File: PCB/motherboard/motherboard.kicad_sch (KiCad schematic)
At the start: 0 parts

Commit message: schematic template added
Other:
- added sheet connectors (connectors.kicad_sch)
- added sheet power (power.kicad_sch)
- title: (none) -> MAIN

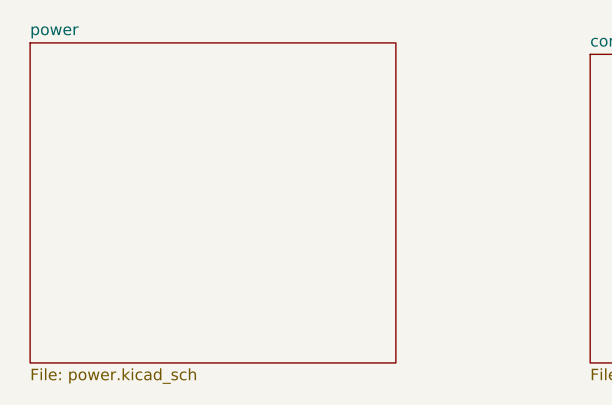
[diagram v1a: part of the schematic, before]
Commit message: started power schematic of pcb
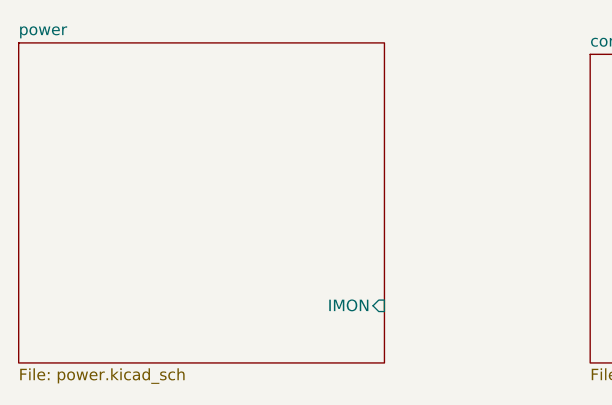
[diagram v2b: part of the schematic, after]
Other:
- sheet power ports: added IMON; removed none
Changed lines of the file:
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@@
 	)
 	(sheet
-		(at 85.09 49.53)
+		(at 83.82 49.53)
 		(size 40.64 35.56)
 		(exclude_from_sim no)
@@
 		)
 		(property "Sheetname" "power"
-			(at 85.09 48.8184 0)
+			(at 83.82 48.8184 0)
 			(effects
 				(font
@@
 		)
 		(property "Sheetfile" "power.kicad_sch"
-			(at 85.09 85.6746 0)
+			(at 83.82 85.6746 0)
 			(effects
 				(font
@@
 			)
 		)
+		(pin "IMON" input
+			(at 124.46 78.74 0)
+			(effects
+				(font
+					(size 1.27 1.27)
+				)
+				(justify right)
+			)
+		)

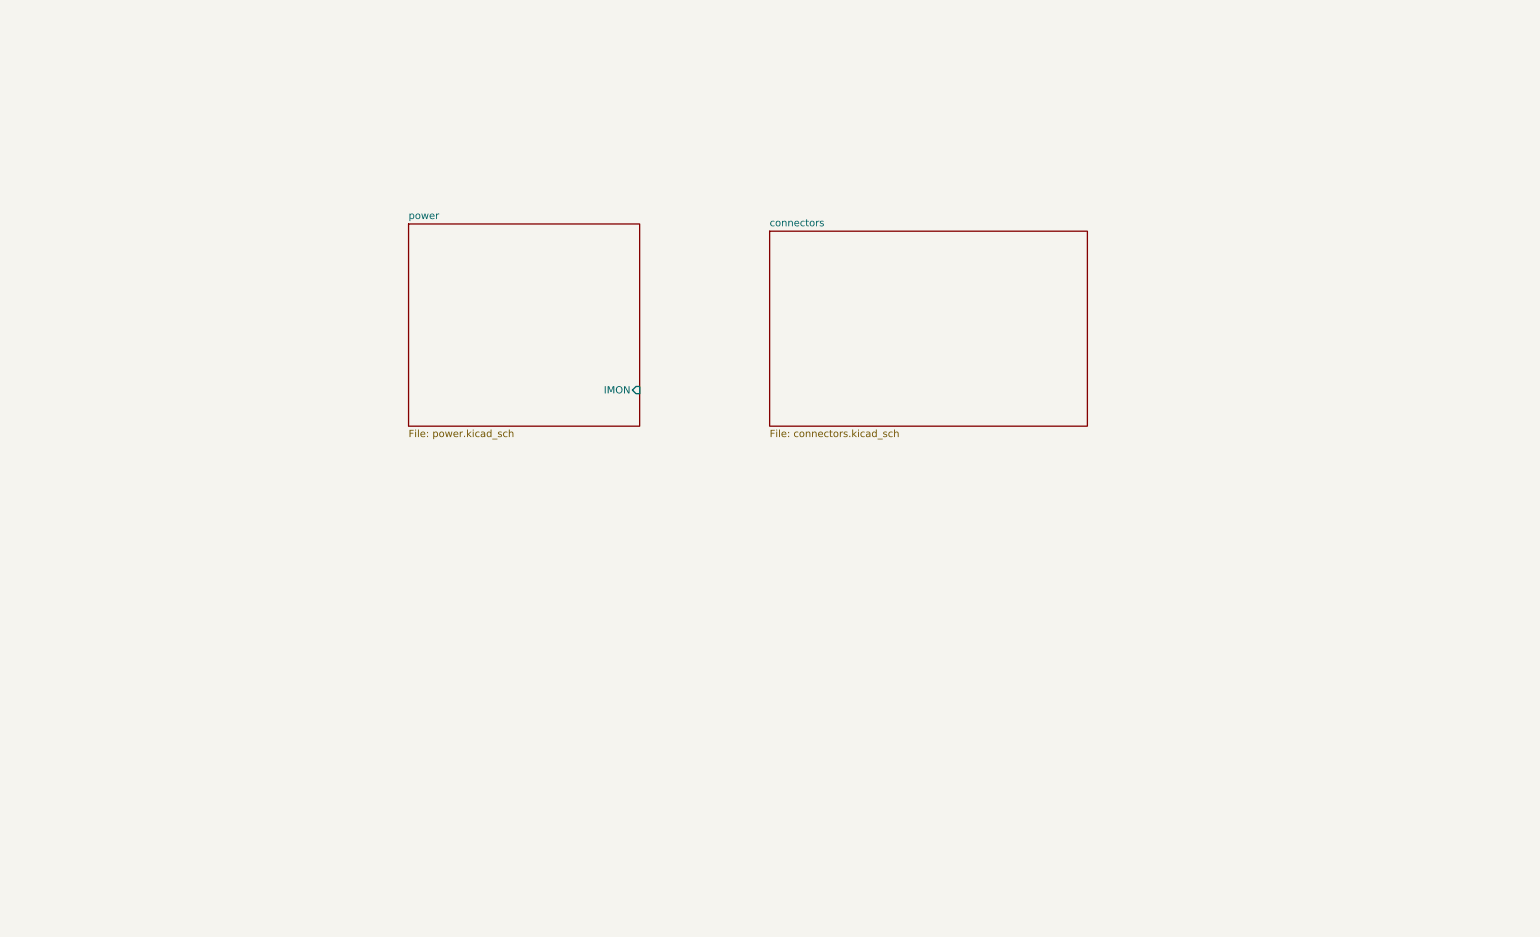
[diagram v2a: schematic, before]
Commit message: updated sch power
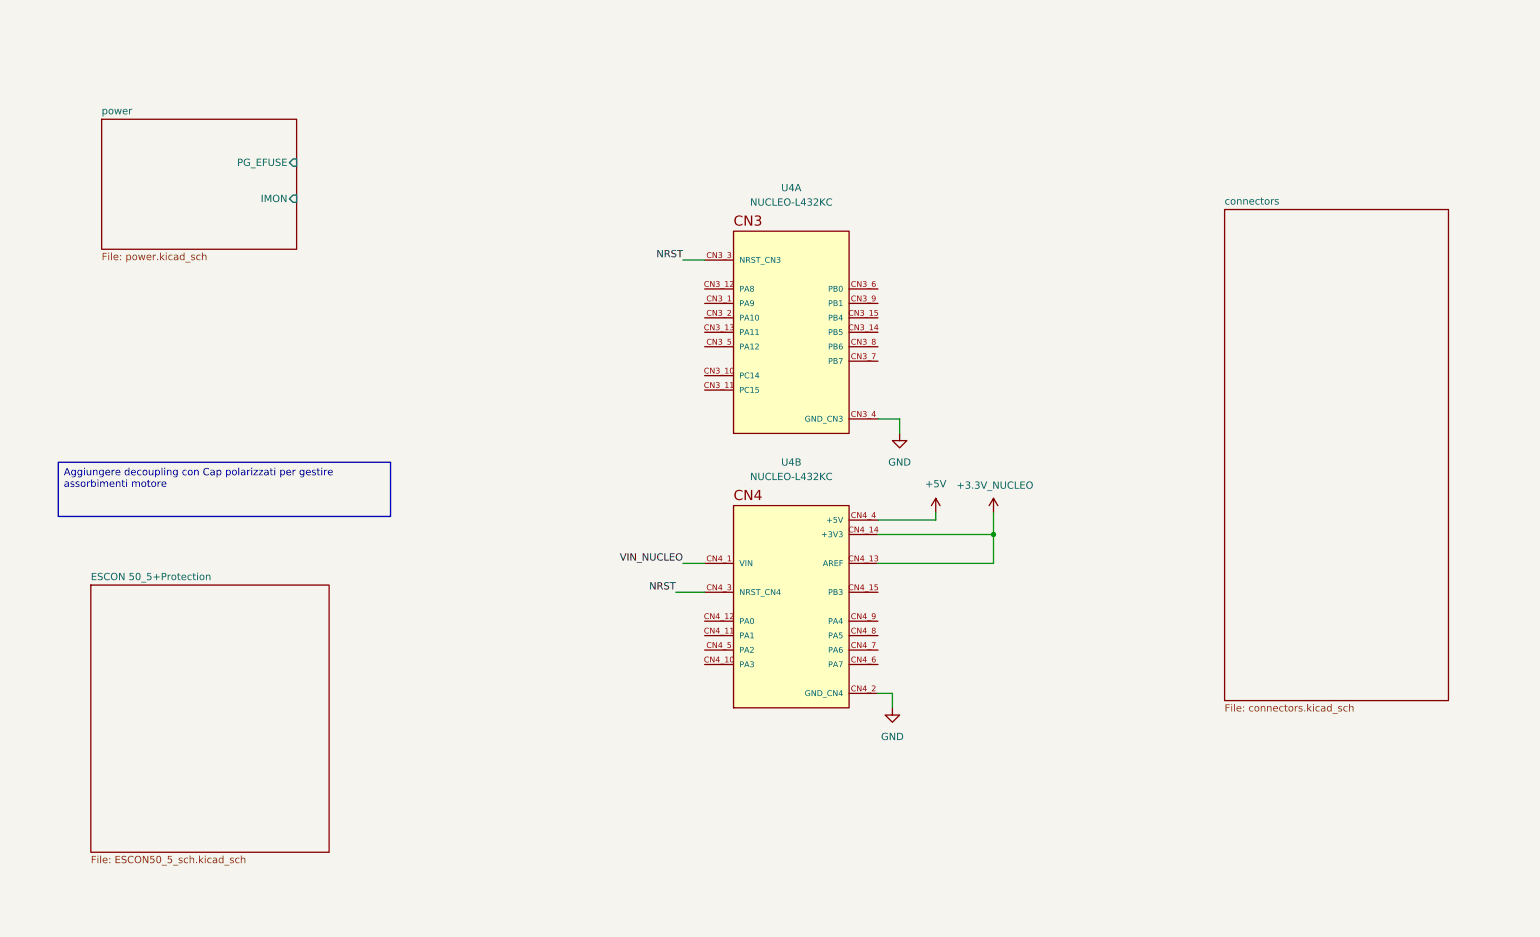
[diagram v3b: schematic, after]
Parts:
- added U4: NUCLEO-L432KC, NUCLEO-L432KC:MODULE_NUCLEO-L432KC, symbol NUCLEO-L432KC:NUCLEO-L432KC
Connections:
- new net +3.3V_NUCLEO: U4.CN4_13 (AREF), U4.CN4_14 (+3V3)
- new net +5V: U4.CN4_4 (+5V)
- new net GND: U4.CN3_4 (GND_CN3), U4.CN4_2 (GND_CN4)
- new net NRST: U4.CN3_3 (NRST_CN3), U4.CN4_3 (NRST_CN4)
- new net VIN_NUCLEO: U4.CN4_1 (VIN)
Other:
- added sheet ESCON 50_5+Protection (ESCON50_5_sch.kicad_sch)
- sheet power ports: added PG_EFUSE; removed none

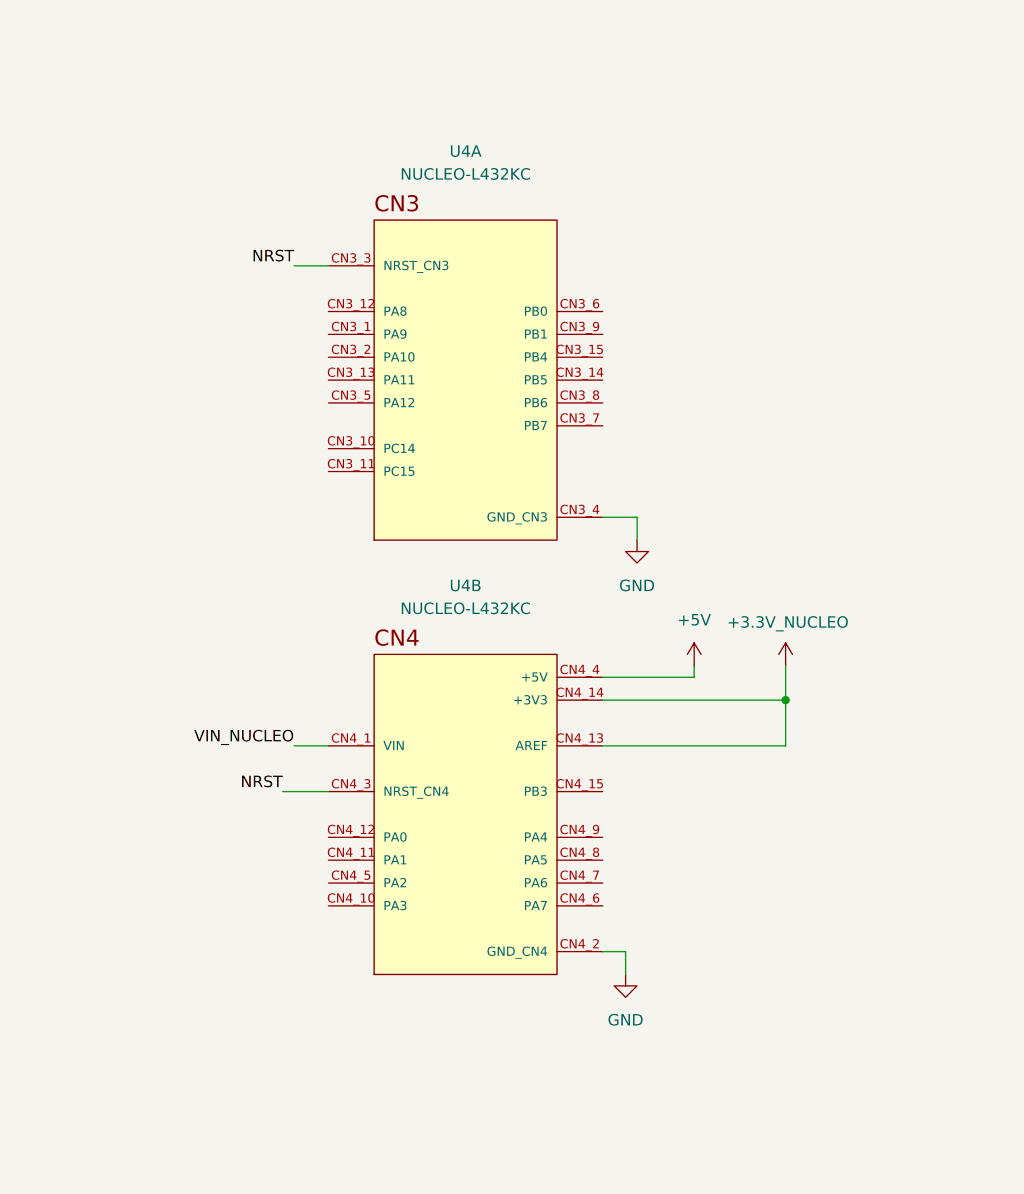
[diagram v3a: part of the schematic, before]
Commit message: aggiunto driver escon in libreria e nel progetto schematico
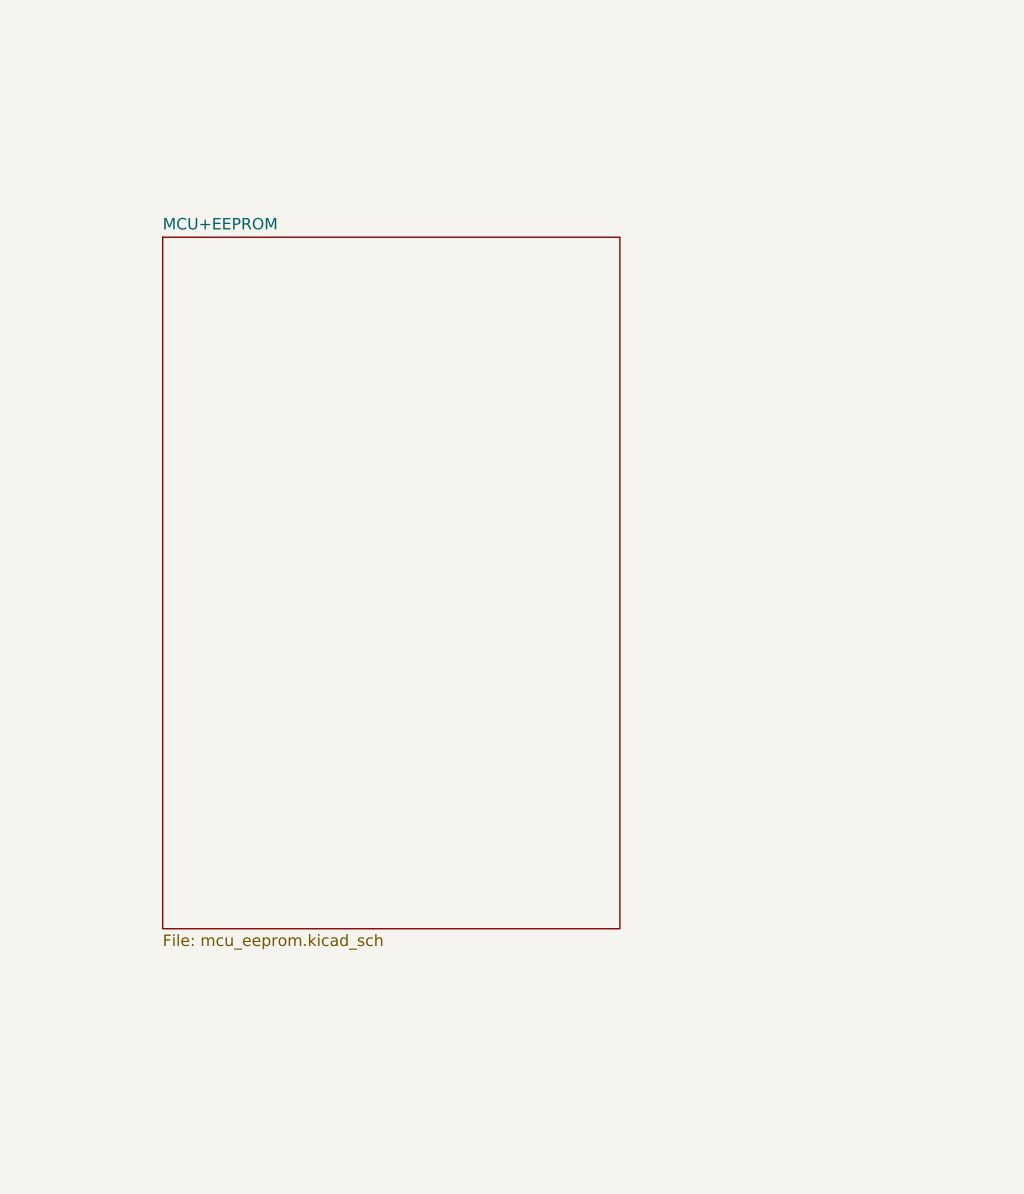
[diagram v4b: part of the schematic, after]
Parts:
- removed U4: NUCLEO-L432KC, NUCLEO-L432KC:MODULE_NUCLEO-L432KC, symbol NUCLEO-L432KC:NUCLEO-L432KC
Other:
- added sheet MCU+EEPROM (mcu_eeprom.kicad_sch)

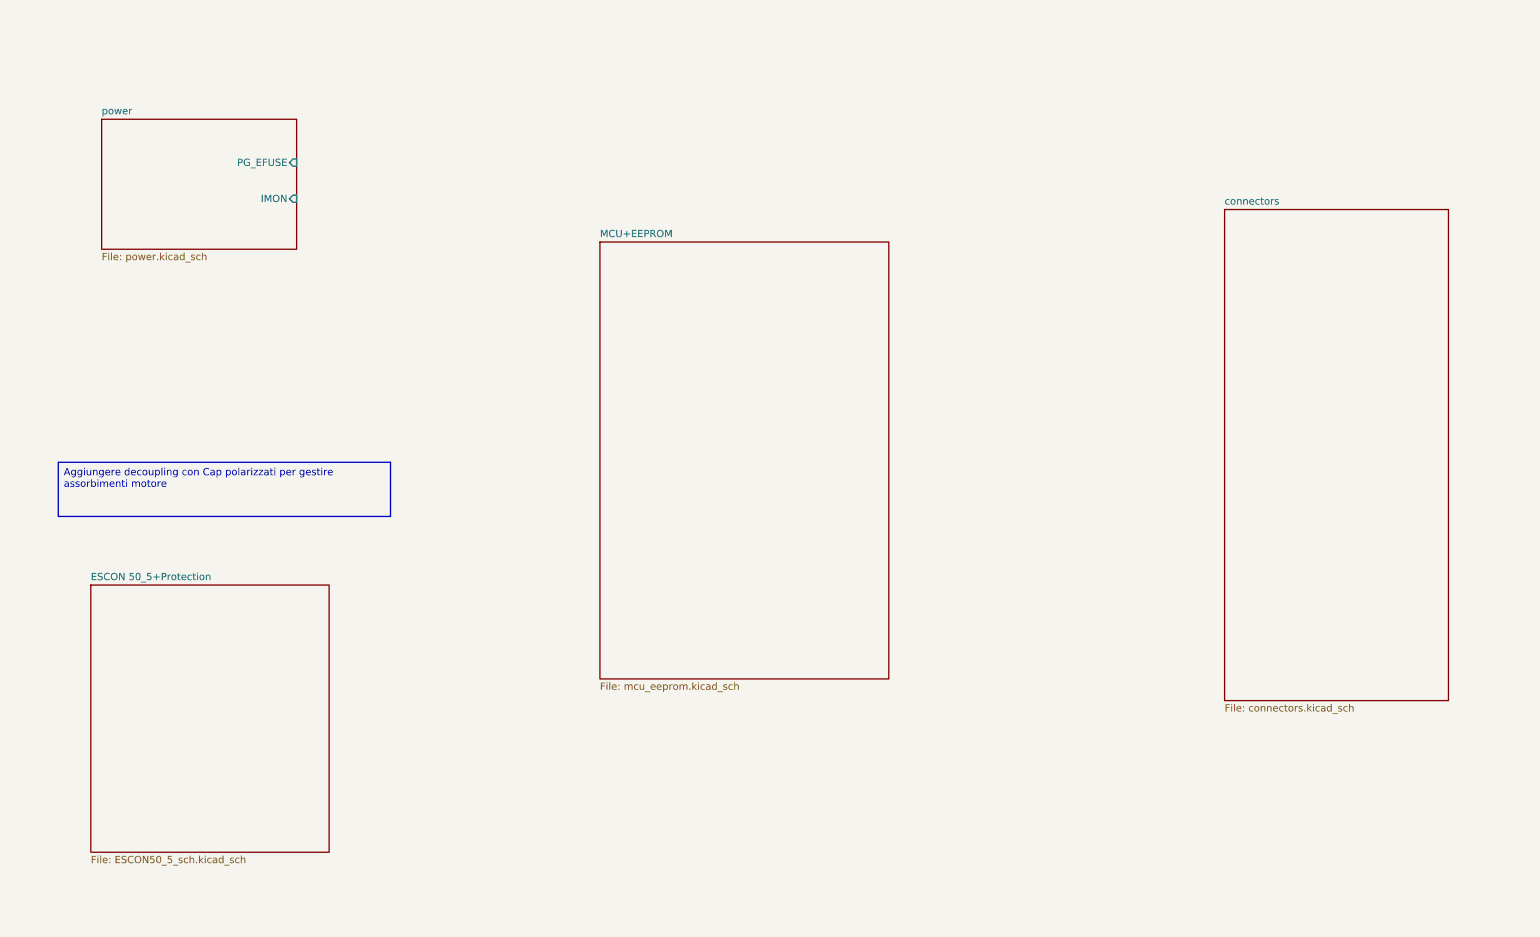
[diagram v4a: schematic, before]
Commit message: reverse current protection on ESCON+others
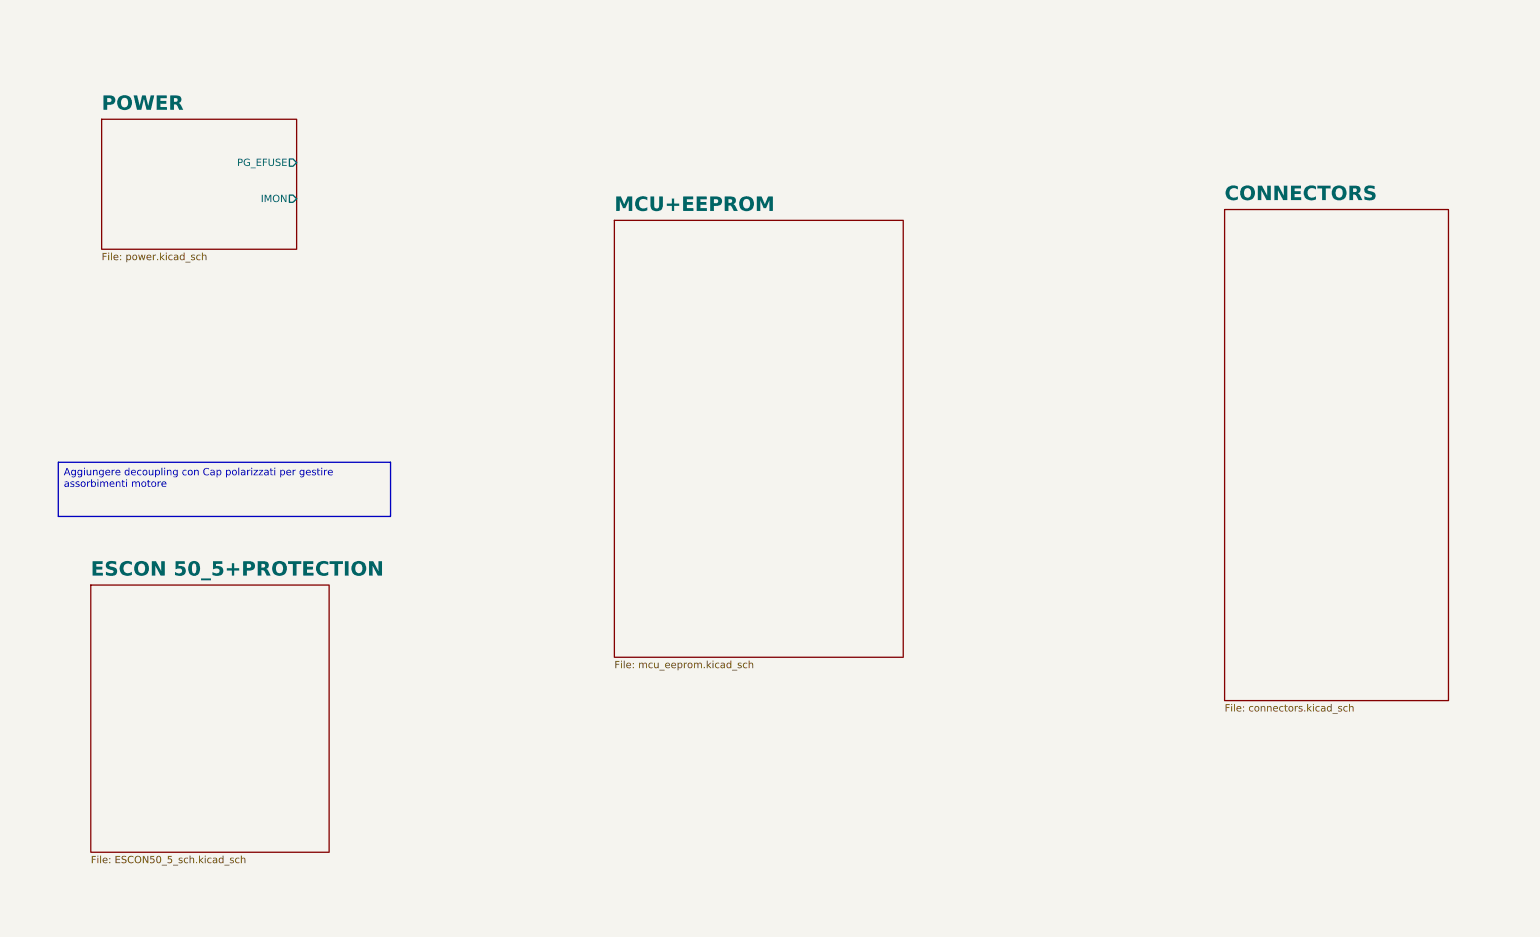
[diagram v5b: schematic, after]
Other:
- sheet ESCON 50_5+Protection renamed ESCON 50_5+PROTECTION
- sheet connectors renamed CONNECTORS
- sheet power renamed POWER
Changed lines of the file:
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@@
 			(color 245 255 30 1.0000)
 		)
-		(property "Sheetname" "ESCON 50_5+Protection"
-			(at 27.94 112.3184 0)
+		(property "Sheetname" "ESCON 50_5+PROTECTION"
+			(at 27.94 111.6834 0)
 			(effects
 				(font
-					(size 1.27 1.27)
+					(size 2.54 2.54)
+					(thickness 0.508)
+					(bold yes)
 				)
 				(justify left bottom)
@@
 			(color 39 240 255 1.0000)
 		)
-		(property "Sheetname" "connectors"
-			(at 227.33 46.2784 0)
+		(property "Sheetname" "CONNECTORS"
+			(at 227.33 45.6434 0)
 			(effects
 				(font
-					(size 1.27 1.27)
+					(size 2.54 2.54)
+					(thickness 0.508)
+					(bold yes)
 				)
 				(justify left bottom)
@@
 	)
 	(sheet
-		(at 117.475 52.705)
+		(at 120.015 48.895)
 		(size 50.8 76.835)
 		(exclude_from_sim no)
@@
 		)
 		(property "Sheetname" "MCU+EEPROM"
-			(at 117.475 51.9934 0)
+			(at 120.015 47.5484 0)
 			(effects
 				(font
-					(size 1.27 1.27)
+					(size 2.54 2.54)
+					(thickness 0.508)
+					(bold yes)
 				)
 				(justify left bottom)
@@
 		)
 		(property "Sheetfile" "mcu_eeprom.kicad_sch"
-			(at 117.475 130.1246 0)
+			(at 120.015 126.3146 0)
 			(effects
 				(font
@@
 			(color 255 171 19 1.0000)
 		)
-		(property "Sheetname" "power"
-			(at 29.845 30.4034 0)
+		(property "Sheetname" "POWER"
+			(at 29.845 29.7684 0)
 			(effects
 				(font
-					(size 1.27 1.27)
+					(size 2.54 2.54)
+					(thickness 0.508)
+					(bold yes)
 				)
 				(justify left bottom)
@@
 			)
 		)
-		(pin "IMON" input
+		(pin "IMON" output
 			(at 64.135 45.085 0)
 			(effects
@@
 			)
 		)
-		(pin "PG_EFUSE" input
+		(pin "PG_EFUSE" output
 			(at 64.135 38.735 0)
 			(effects
